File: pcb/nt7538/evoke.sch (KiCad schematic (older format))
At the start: 17 parts, among them U1 STM32F103C8Tx

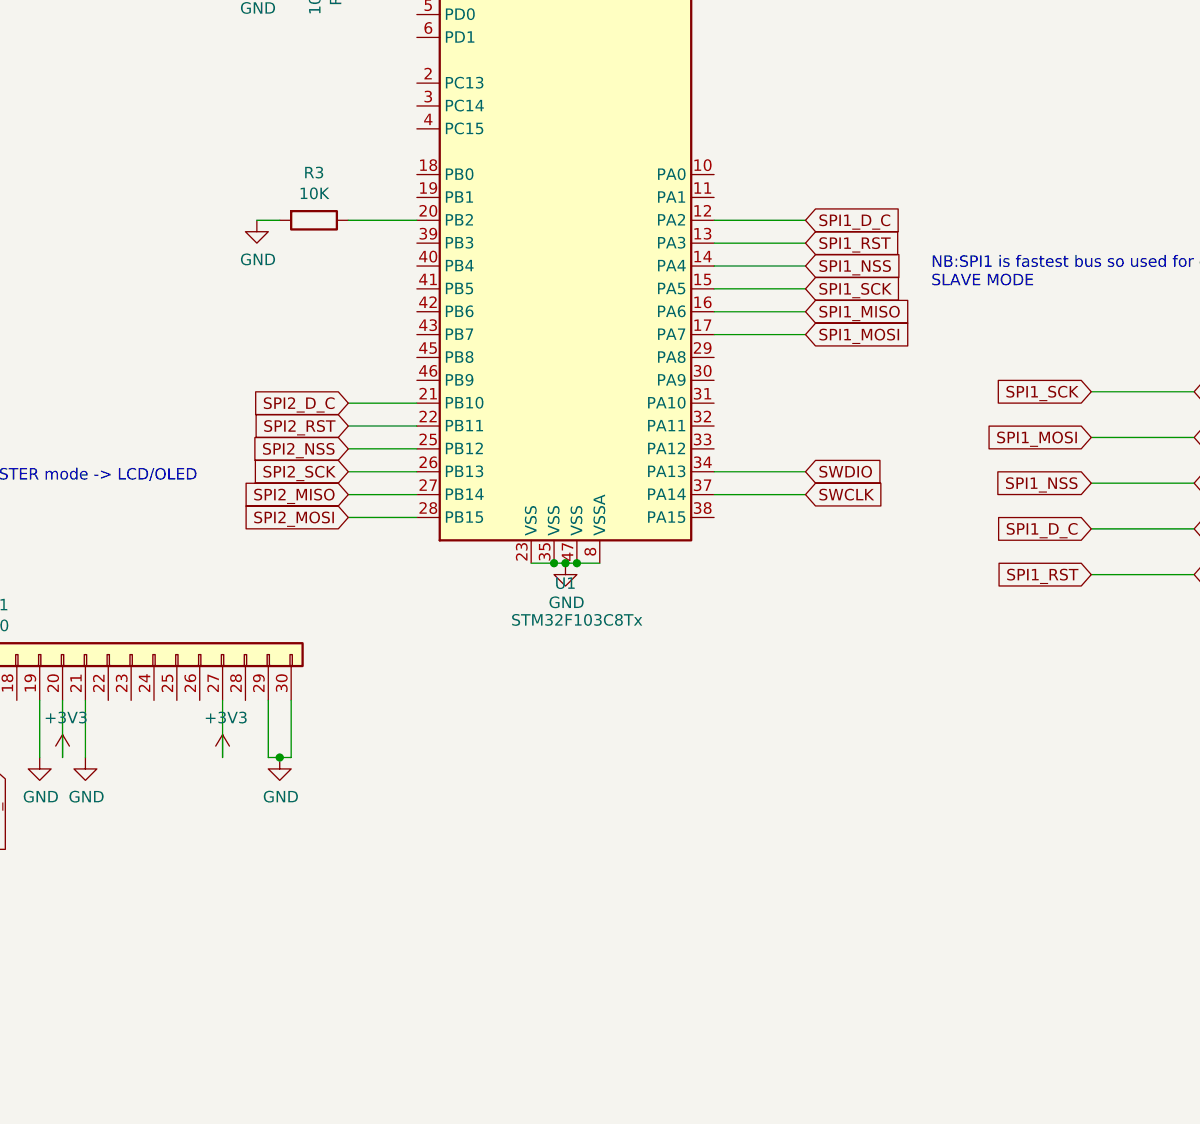
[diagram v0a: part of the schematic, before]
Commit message: Initial draft of backlight PWM control
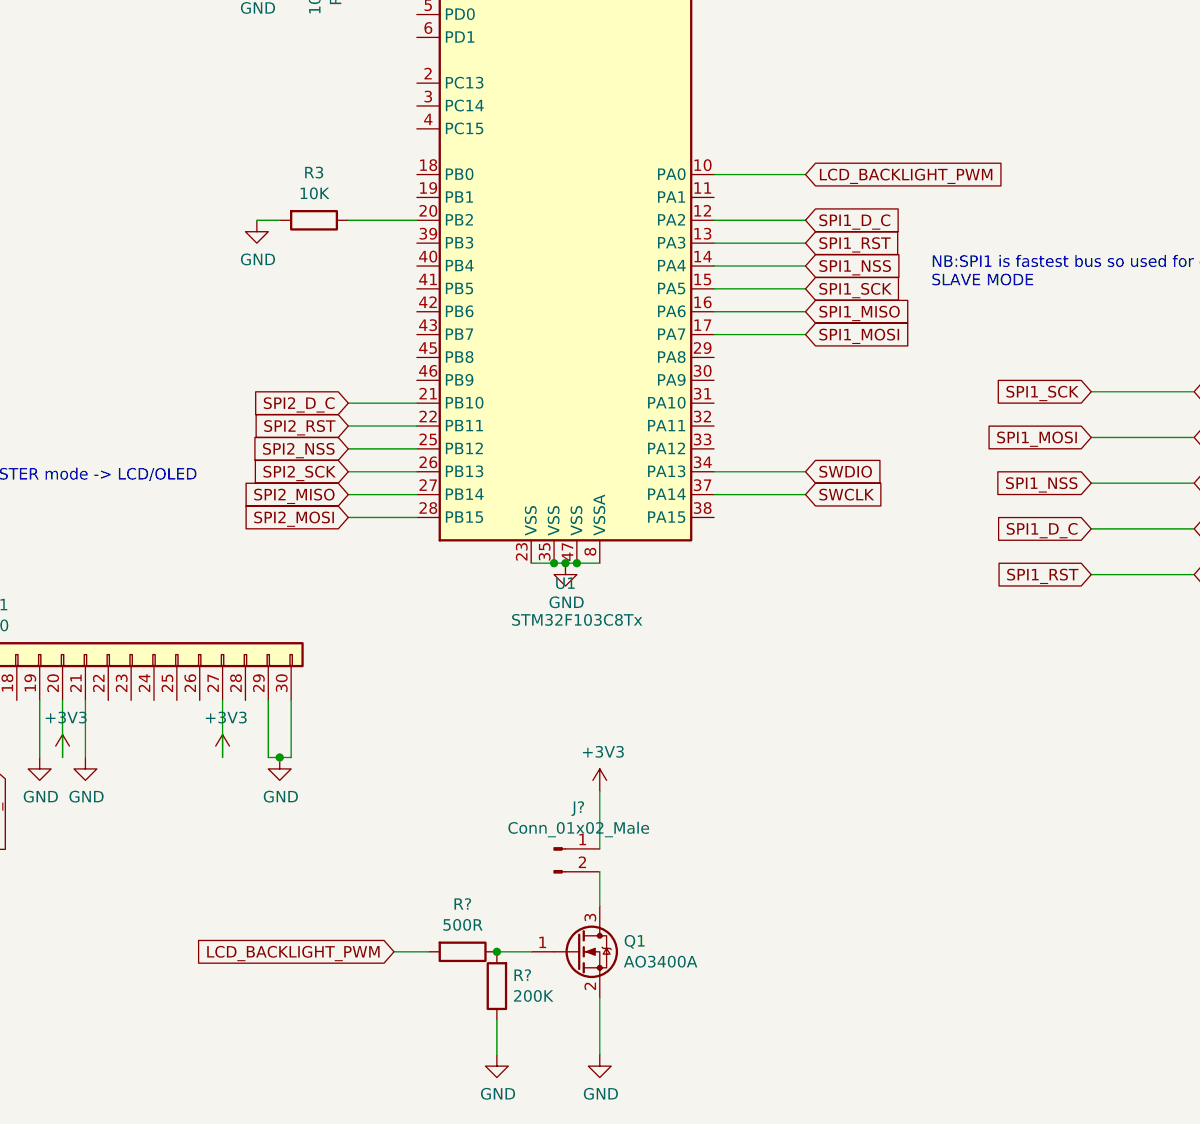
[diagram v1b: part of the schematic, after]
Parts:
- added J?: Conn_01x02_Male, symbol Connector:Conn_01x02_Male
- added Q1: AO3400A, Package_TO_SOT_SMD:SOT-23, symbol Device:Q_NMOS_GSD
- added R?: 500R, symbol Device:R
- added R?: 200K, symbol Device:R
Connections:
- net +3V3: now also J?.1 (Pin_1)
- net GND: now also Q1.2 (S), R?.1
- net LCD_BACKLIGHT_PWM: now reaches U1.10 (PA0)
- net LCD_BACKLIGHT_PWM: now also R?.2
- new net: Q1.1 (G), R?.1, R?.2
- new net: J?.2 (Pin_2), Q1.3 (D)
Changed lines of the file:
@@
 Wire Wire Line
 	9850 2150 10000 2150
+$Comp
+L Device:Q_NMOS_GSD Q1
+U 1 1 5EC74373
+P 5750 6100
+F 0 "Q1" H 5955 6146 50  0000 L CNN
+F 1 "AO3400A" H 5955 6055 50  0000 L CNN
+F 2 "Package_TO_SOT_SMD:SOT-23" H 5950 6200 50  0001 C CNN
+F 3 "~" H 5750 6100 50  0001 C CNN
+	1    5750 6100
+	1    0    0    -1
+$EndComp
+$Comp
+L power:GND #PWR?
+U 1 1 5EC7A582
+P 5850 6550
+F 0 "#PWR?" H 5850 6300 50  0001 C CNN
+F 1 "GND" H 5855 6377 50  0000 C CNN
+F 2 "" H 5850 6550 50  0001 C CNN
+F 3 "" H 5850 6550 50  0001 C CNN
+	1    5850 6550
+	1    0    0    -1
+$EndComp
+Wire Wire Line
+	5850 6550 5850 6300
+$Comp
+L Device:R R?
+U 1 1 5EC7E7FC
+P 5250 6100
+F 0 "R?" V 5043 6100 50  0000 C CNN
+F 1 "500R" V 5134 6100 50  0000 C CNN
+F 2 "" V 5180 6100 50  0001 C CNN
+F 3 "~" H 5250 6100 50  0001 C CNN
+	1    5250 6100
+	0    1    1    0
+$EndComp
+Wire Wire Line
+	5550 6100 5400 6100
+Connection ~ 5400 6100
+$Comp
+L power:GND #PWR?
+U 1 1 5EC8F417
+P 5400 6550
+F 0 "#PWR?" H 5400 6300 50  0001 C CNN
+F 1 "GND" H 5405 6377 50  0000 C CNN
+F 2 "" H 5400 6550 50  0001 C CNN
+F 3 "" H 5400 6550 50  0001 C CNN
+	1    5400 6550
+	1    0    0    -1
+$EndComp
+Wire Wire Line
+	5400 6550 5400 6400
+Wire Wire Line
+	5100 6100 4950 6100
+$Comp
+L Connector:Conn_01x02_Male J?
+U 1 1 5EC97737
+P 5650 5650
+F 0 "J?" H 5758 5831 50  0000 C CNN
+F 1 "Conn_01x02_Male" H 5758 5740 50  0000 C CNN
+F 2 "" H 5650 5650 50  0001 C CNN
+F 3 "~" H 5650 5650 50  0001 C CNN
+	1    5650 5650
+	1    0    0    -1
+$EndComp
+Wire Wire Line
+	5850 5750 5850 5900
+Wire Wire Line
+	5850 5650 5850 5400
+$Comp
+L evoke-rescue:+3V3-power #PWR?
+U 1 1 5EC9F2F0
+P 5850 5400
+F 0 "#PWR?" H 5850 5250 50  0001 C CNN
+F 1 "+3V3" H 5865 5573 50  0000 C CNN
+F 2 "" H 5850 5400 50  0001 C CNN
+F 3 "" H 5850 5400 50  0001 C CNN
+	1    5850 5400
+	1    0    0    -1
+$EndComp
+$Comp
+L Device:R R?
+U 1 1 5EC825EF
+P 5400 6250
+F 0 "R?" H 5330 6204 50  0000 R CNN
+F 1 "200K" H 5330 6295 50  0000 R CNN
+F 2 "" V 5330 6250 50  0001 C CNN
+F 3 "~" H 5400 6250 50  0001 C CNN
+	1    5400 6250
+	-1   0    0    1
+$EndComp
+Text GLabel 4950 6100 0    50   Input ~ 0
+LCD_BACKLIGHT_PWM
+Text GLabel 6750 2700 2    50   Input ~ 0
+LCD_BACKLIGHT_PWM
+Wire Wire Line
+	6750 2700 6350 2700
 $EndSCHEMATC

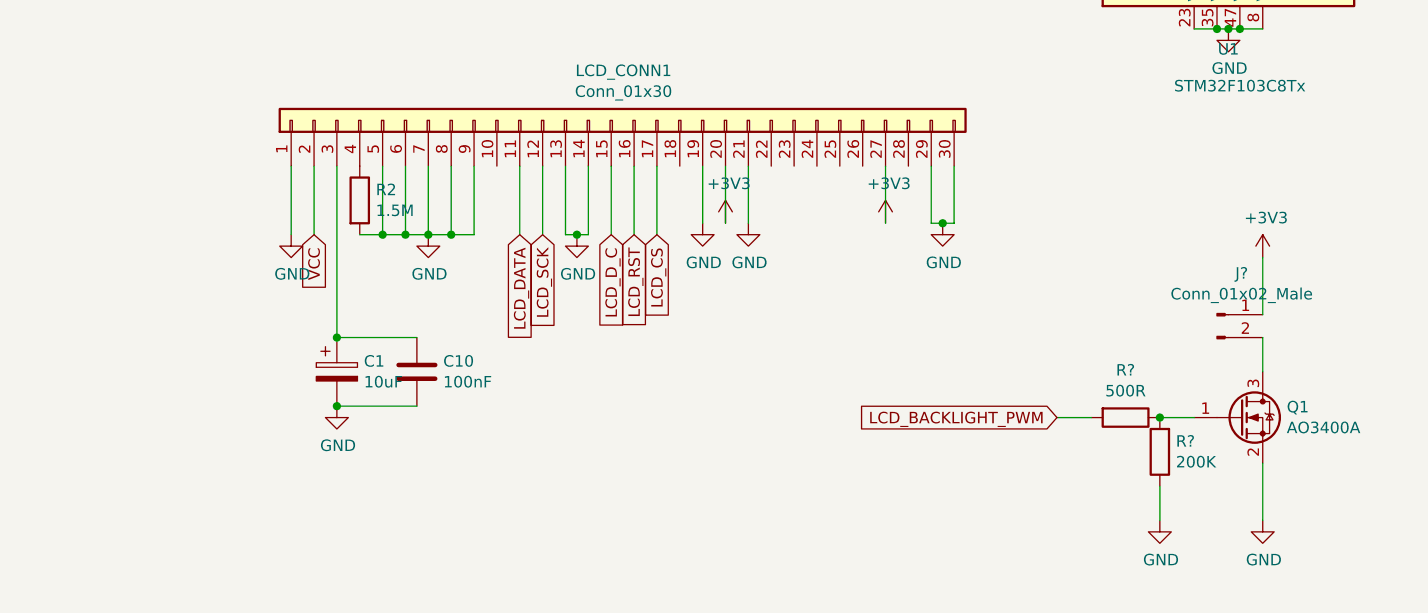
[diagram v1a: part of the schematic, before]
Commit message: Initial changes for LCD support
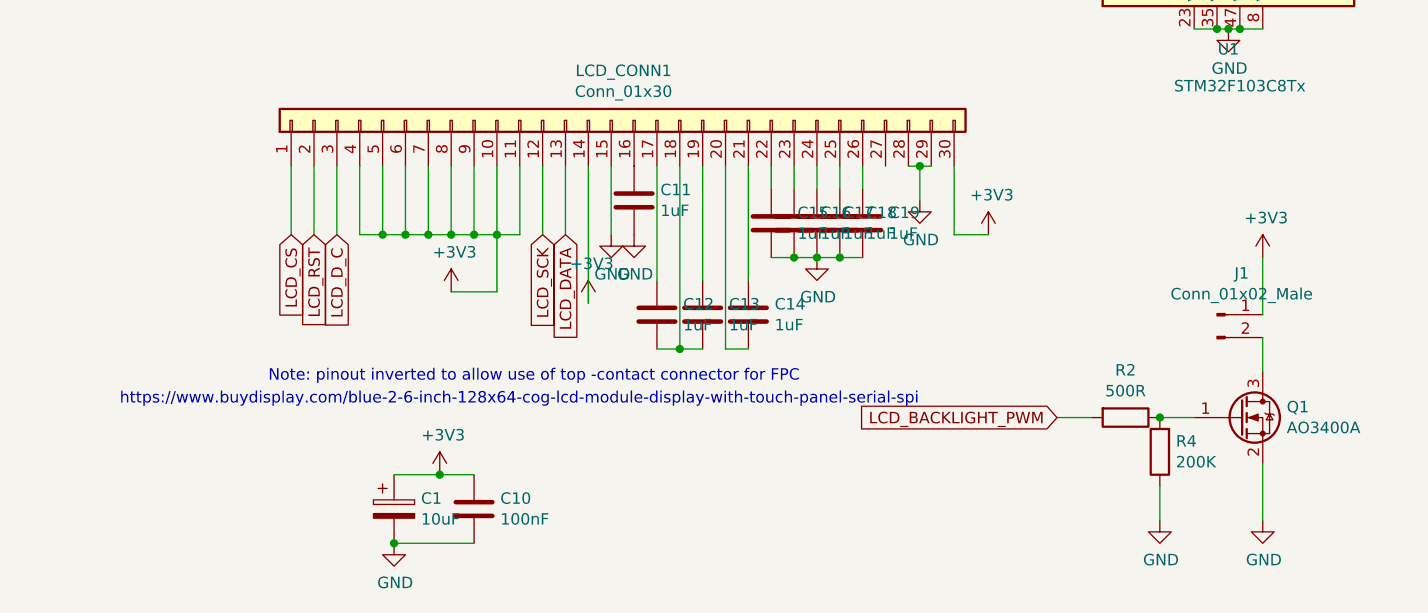
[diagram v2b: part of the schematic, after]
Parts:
- removed R2: 1.5M, Resistor_SMD:R_0805_2012Metric, symbol evoke-rescue:R-Device
- added C11, C12, C13, C14, C15, C16, C17, C18, C19: 1uF, Capacitor_SMD:C_0805_2012Metric, symbol Device:C
- R2, R4: renamed from R?; footprint (none) -> Resistor_SMD:R_0805_2012Metric
- gave numbers to parts that had none: 1
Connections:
- net +3V3: now also C1.1, C10.1, LCD_CONN1.10 (Pin_10), LCD_CONN1.11 (Pin_11), LCD_CONN1.14 (Pin_14), LCD_CONN1.30 (Pin_30), LCD_CONN1.4 (Pin_4), LCD_CONN1.5 (Pin_5), LCD_CONN1.6 (Pin_6), LCD_CONN1.7 (Pin_7), LCD_CONN1.8 (Pin_8), LCD_CONN1.9 (Pin_9); no longer LCD_CONN1.20 (Pin_20), LCD_CONN1.27 (Pin_27)
- net GND: now also LCD_CONN1.15 (Pin_15), LCD_CONN1.28 (Pin_28), C11.2, C15.2, C16.2, C17.2, C18.2, C19.2; no longer LCD_CONN1.1 (Pin_1), LCD_CONN1.13 (Pin_13), LCD_CONN1.14 (Pin_14), LCD_CONN1.19 (Pin_19), LCD_CONN1.21 (Pin_21), LCD_CONN1.30 (Pin_30), LCD_CONN1.5 (Pin_5), LCD_CONN1.6 (Pin_6), LCD_CONN1.7 (Pin_7), LCD_CONN1.8 (Pin_8), LCD_CONN1.9 (Pin_9)
- net LCD_CS: now also LCD_CONN1.1 (Pin_1); no longer LCD_CONN1.17 (Pin_17)
- net LCD_DATA: now also LCD_CONN1.13 (Pin_13); no longer LCD_CONN1.11 (Pin_11)
- net LCD_D_C: now also LCD_CONN1.3 (Pin_3); no longer LCD_CONN1.15 (Pin_15)
- net LCD_RST: now also LCD_CONN1.2 (Pin_2); no longer LCD_CONN1.16 (Pin_16)
- net VCC: no longer LCD_CONN1.2 (Pin_2)
- net at LCD_CONN1.18 (Pin_18): now also C12.2, C13.2
- net at LCD_CONN1.22 (Pin_22): now also C15.1
- net at LCD_CONN1.23 (Pin_23): now also C16.1
- net at LCD_CONN1.24 (Pin_24): now also C17.1
- net at LCD_CONN1.25 (Pin_25): now also C18.1
- net at LCD_CONN1.26 (Pin_26): now also C19.1
- new net: C11.1, LCD_CONN1.16 (Pin_16)
- new net: C12.1, LCD_CONN1.17 (Pin_17)
- new net: C13.1, LCD_CONN1.19 (Pin_19)
- new net: C14.2, LCD_CONN1.20 (Pin_20)
- new net: C14.1, LCD_CONN1.21 (Pin_21)
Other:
- note added: "Note: pinout inverted to allow use of top -contact connector for FPC"
- note added: "https://www.buydisplay.com/blue-2-6-inch-128x64-cog-lcd-module-display-with-touch-panel-serial-spi"
- moved on the sheet: C1, C10

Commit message: Put next revision into manufacture - hopefully ready to go, now with test points!
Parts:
- J1: footprint (none) -> Connector_JST:JST_PH_B2B-PH-SM4-TB_1x02-1MP_P2.00mm_Vertical
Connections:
- net +3V3: now also J1.2 (Pin_2); no longer J1.1 (Pin_1)
- net at Q1.3 (D): now also J1.1 (Pin_1); no longer J1.2 (Pin_2)
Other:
- moved on the sheet: J1
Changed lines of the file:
@@
 Wire Wire Line
 	5100 6100 4950 6100
-$Comp
-L Connector:Conn_01x02_Male J1
-U 1 1 5EC97737
-P 5650 5650
-F 0 "J1" H 5758 5831 50  0000 C CNN
-F 1 "Conn_01x02_Male" H 5758 5740 50  0000 C CNN
-F 2 "" H 5650 5650 50  0001 C CNN
-F 3 "~" H 5650 5650 50  0001 C CNN
-	1    5650 5650
-	1    0    0    -1
-$EndComp
 Wire Wire Line
 	5850 5750 5850 5900
@@
 	1    0    0    -1
 $EndComp
+$Comp
+L Connector:Conn_01x02_Male J1
+U 1 1 5EC97737
+P 6050 5750
+F 0 "J1" H 6158 5931 50  0000 C CNN
+F 1 "Conn_01x02_Male" H 6158 5840 50  0000 C CNN
+F 2 "Connector_JST:JST_PH_B2B-PH-SM4-TB_1x02-1MP_P2.00mm_Vertical" H 6050 5750 50  0001 C CNN
+F 3 "~" H 6050 5750 50  0001 C CNN
+	1    6050 5750
+	-1   0    0    1
+$EndComp
 $EndSCHEMATC

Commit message: Commit of NT version including trimpot
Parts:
- removed C1: 10uF, Capacitor_Tantalum_SMD:CP_EIA-3216-18_Kemet-A, symbol evoke-rescue:CP-Device
- removed C10: 100nF, Capacitor_SMD:C_0805_2012Metric, symbol evoke-rescue:C-Device
- removed C11, C12, C13, C14, C15, C16, C17, C18, C19: 1uF, Capacitor_SMD:C_0805_2012Metric, symbol Device:C
- removed J1: Conn_01x02_Male, Connector_JST:JST_PH_B2B-PH-SM4-TB_1x02-1MP_P2.00mm_Vertical, symbol Connector:Conn_01x02_Male
- removed R2: 500R, Resistor_SMD:R_0805_2012Metric, symbol Device:R
- removed R4: 200K, Resistor_SMD:R_0805_2012Metric, symbol Device:R
- added C1, C10, C11, C14, C15, C16, C17, C18, C19: 1uF, Capacitor_SMD:C_0805_2012Metric, symbol evoke-rescue:C-Device-evoke-rescue
- added C12: 100nF, Capacitor_SMD:C_0805_2012Metric, symbol evoke-rescue:C-Device-evoke-rescue
- added C13: 4.7uF, Capacitor_SMD:C_0805_2012Metric, symbol evoke-rescue:C-Device-evoke-rescue
- added J1: Conn_01x03_Male, Connector_PinHeader_2.54mm:PinHeader_1x03_P2.54mm_Vertical, symbol evoke-rescue:Conn_01x03_Male-Connector-evoke-rescue
- added J2: BACKLIGHT_CONN, Connector_JST:JST_PH_S2B-PH-SM4-TB_1x02-1MP_P2.00mm_Horizontal, symbol Connector:Conn_01x02_Male
- added J3: SUPP_PWR, Connector_PinHeader_2.54mm:PinHeader_1x02_P2.54mm_Vertical, symbol Connector:Conn_01x02_Male
- added R2: 500R, Resistor_SMD:R_0805_2012Metric, symbol evoke-rescue:R-Device-evoke-rescue
- added R4: 200K, Resistor_SMD:R_0805_2012Metric, symbol evoke-rescue:R-Device-evoke-rescue
- added TP1, TP2, TP3, TP4, TP5, TP6, TP7, TP8: TestPoint, TestPoint:TestPoint_Pad_D1.0mm, symbol evoke-rescue:TestPoint-Connector-evoke-rescue
- added VR_CONTRAST1: 100K, Potentiometer_THT:Potentiometer_Vishay_T73YP_Vertical, symbol Device:R_POT
- C2: symbol evoke-rescue:CP-Device -> evoke-rescue:CP-Device-evoke-rescue
- C3, C4, C5, C6, C7, C8, C9: symbol evoke-rescue:C-Device -> evoke-rescue:C-Device-evoke-rescue
- INPUT_CONN1: symbol evoke-rescue:Conn_01x08-Connector_Generic -> evoke-rescue:Conn_01x08-Connector_Generic-evoke-rescue
- LCD_CONN1: symbol evoke-rescue:Conn_01x30-Connector_Generic -> evoke-rescue:Conn_01x30-Connector_Generic-evoke-rescue
- Q1: value AO3400A -> Q_NMOS_GSD; LCSC (none) -> C347475
- R1, R3: symbol evoke-rescue:R-Device -> evoke-rescue:R-Device-evoke-rescue
- ST_LINK1: symbol evoke-rescue:Conn_01x05-Connector_Generic -> evoke-rescue:Conn_01x05-Connector_Generic-evoke-rescue
- U1: symbol evoke-rescue:STM32F103C8Tx-MCU_ST_STM32F1 -> evoke-rescue:STM32F103C8Tx-MCU_ST_STM32F1-evoke-rescue
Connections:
- net +3V3: now also LCD_CONN1.1 (Pin_1), LCD_CONN1.17 (Pin_17), LCD_CONN1.20 (Pin_20), LCD_CONN1.21 (Pin_21), LCD_CONN1.22 (Pin_22), LCD_CONN1.23 (Pin_23), LCD_CONN1.24 (Pin_24), LCD_CONN1.25 (Pin_25), LCD_CONN1.26 (Pin_26), LCD_CONN1.27 (Pin_27), C12.1, C13.1, J2.1 (Pin_1), J3.1 (Pin_1), VR_CONTRAST1.1; no longer LCD_CONN1.10 (Pin_10), LCD_CONN1.11 (Pin_11), LCD_CONN1.14 (Pin_14), LCD_CONN1.30 (Pin_30), LCD_CONN1.4 (Pin_4), LCD_CONN1.5 (Pin_5), LCD_CONN1.6 (Pin_6), LCD_CONN1.7 (Pin_7), LCD_CONN1.8 (Pin_8), LCD_CONN1.9 (Pin_9)
- net CS_IN: now also TP3.1
- net D_C_IN: now also TP4.1
- net GND: now also LCD_CONN1.16 (Pin_16), LCD_CONN1.2 (Pin_2), LCD_CONN1.3 (Pin_3), C1.2, C12.2, C13.2, C15.2, C16.2, C17.2, C18.2, C19.2, J1.3 (Pin_3), J3.2 (Pin_2), R4.2, VR_CONTRAST1.3; no longer LCD_CONN1.15 (Pin_15), LCD_CONN1.28 (Pin_28), LCD_CONN1.29 (Pin_29)
- net LCD_BACKLIGHT_PWM: now also U1.19 (PB1), R2.2; no longer U1.10 (PA0)
- net LCD_CS: now also LCD_CONN1.30 (Pin_30), TP7.1; no longer LCD_CONN1.1 (Pin_1)
- net LCD_DATA: now also LCD_CONN1.18 (Pin_18), TP6.1; no longer LCD_CONN1.13 (Pin_13)
- net LCD_D_C: now also LCD_CONN1.28 (Pin_28), TP8.1; no longer LCD_CONN1.3 (Pin_3)
- net LCD_RST: now also LCD_CONN1.29 (Pin_29); no longer LCD_CONN1.2 (Pin_2)
- net LCD_SCK: now also LCD_CONN1.19 (Pin_19), TP5.1; no longer LCD_CONN1.12 (Pin_12)
- net SCK_IN: now also TP1.1
- net SDIN_IN: now also TP2.1
- net at U1.18 (PB0): now also VR_CONTRAST1.2
- net USART1_TX: now reaches U1.30 (PA9)
- net USART1_TX: now also J1.1 (Pin_1)
- net USART1_RX: now reaches U1.31 (PA10)
- net USART1_RX: now also J1.2 (Pin_2)
- net at Q1.1 (G): now also R2.1, R4.1
- net at Q1.3 (D): now also J2.2 (Pin_2)
- new net: C14.2, LCD_CONN1.10 (Pin_10)
- new net: C14.1, LCD_CONN1.11 (Pin_11)
- new net: C10.1, LCD_CONN1.12 (Pin_12)
- new net: C10.2, C11.2, LCD_CONN1.13 (Pin_13)
- new net: C11.1, LCD_CONN1.14 (Pin_14)
- new net: C1.1, LCD_CONN1.15 (Pin_15)
- new net: C15.1, LCD_CONN1.5 (Pin_5)
- new net: C16.1, LCD_CONN1.6 (Pin_6)
- new net: C17.1, LCD_CONN1.7 (Pin_7)
- new net: C18.1, LCD_CONN1.8 (Pin_8)
- new net: C19.1, LCD_CONN1.9 (Pin_9)
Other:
- note removed: "Note: pinout inverted to allow use of top -contact connector for FPC"
- moved on the sheet: LCD_CONN1
